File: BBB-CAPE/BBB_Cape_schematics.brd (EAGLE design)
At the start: 160 x 100 mm, 81 parts, among them IC1 EEPROM-I2CSMD, SW2 219-02

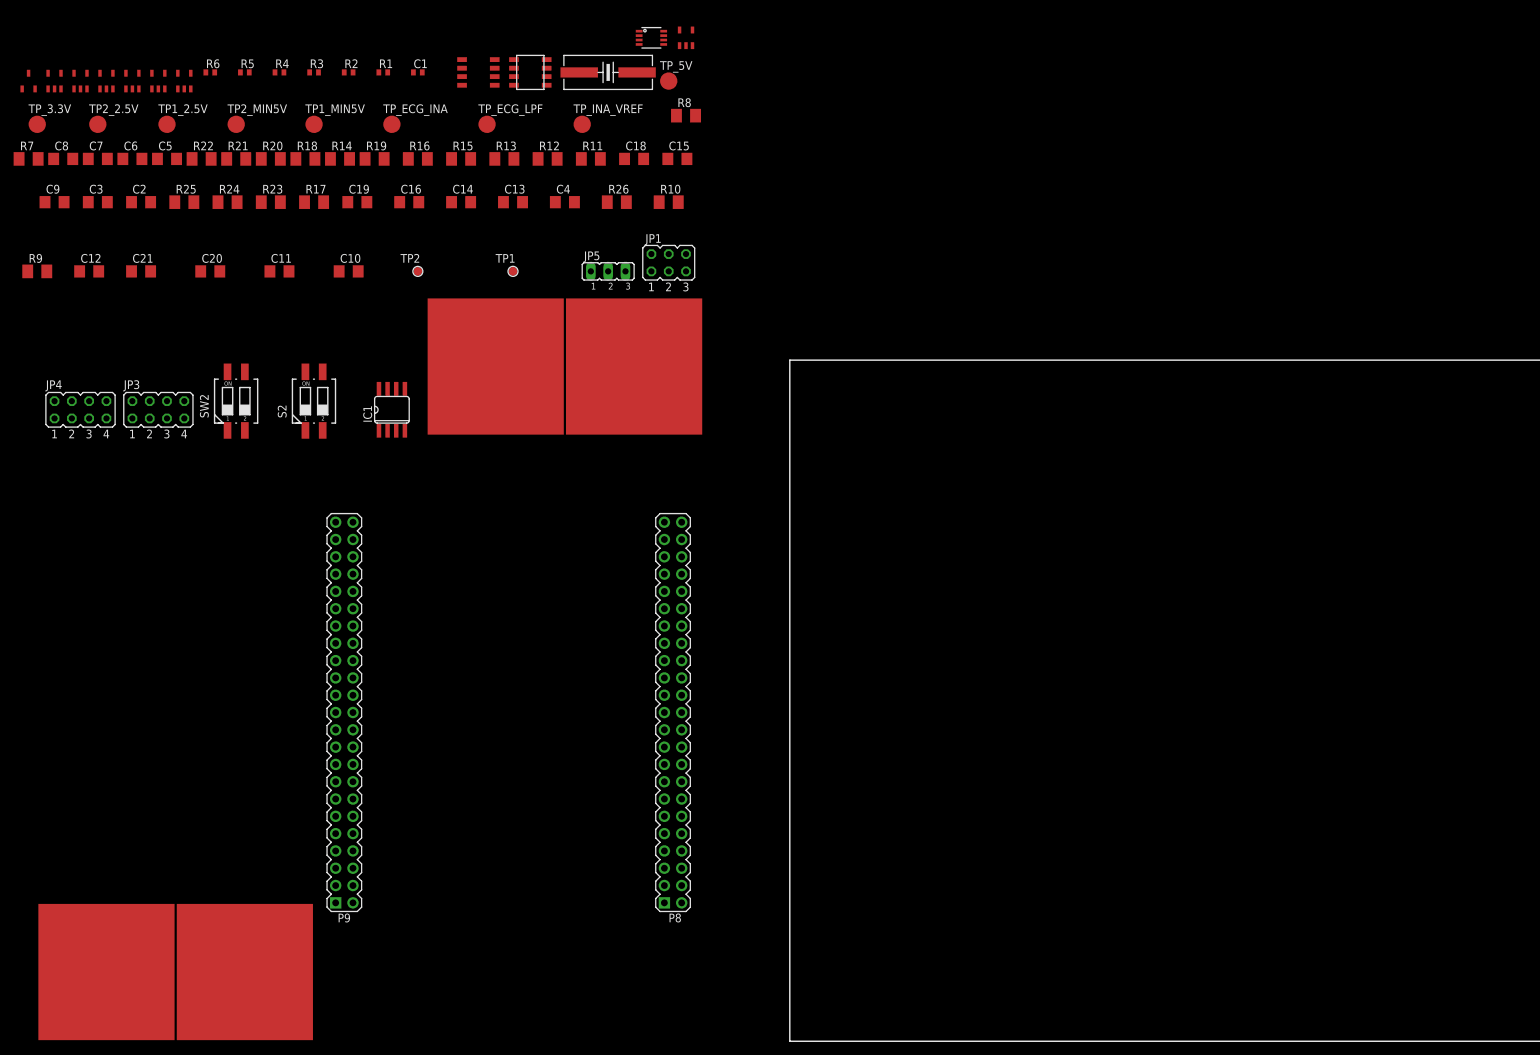
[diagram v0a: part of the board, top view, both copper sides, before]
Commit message: Placement of components in BBB_Cape_schematics.brd, removed ERC erros in BBB_Cape_schematics.sch and Add sign in INA129 to identify pin no 1 in Components.lbr
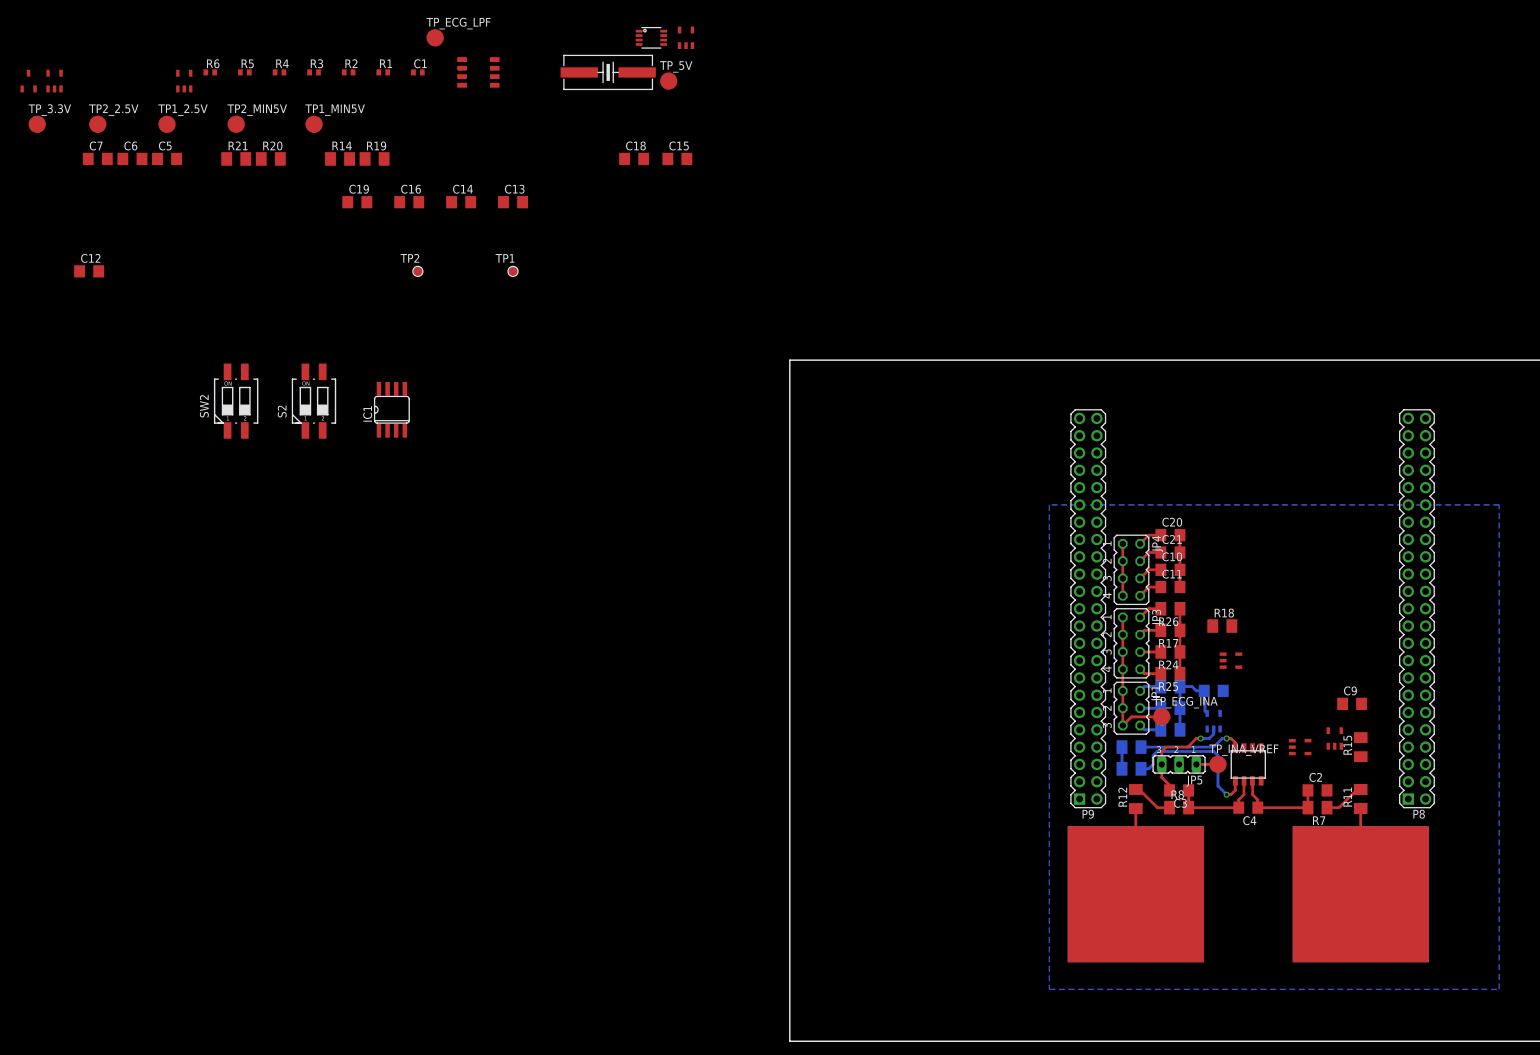
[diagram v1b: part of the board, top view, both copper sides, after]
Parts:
- U$4: device Components:INA129 -> Components:INA129@1
- moved R7 211.9 mm to (77.5, 34.3), turned to 180 degrees
- moved U$12 204.5 mm to (80.0, 44.5)
- moved C9 204.2 mm to (82.5, 49.5)
- moved U$11 197.4 mm to (74.9, 43.2), turned to 270 degrees
- moved C2 193.1 mm to (77.5, 36.8)
- moved U$13 189.1 mm to (64.8, 55.9), turned to 270 degrees
- moved C8 186.1 mm to (62.2, 51.4), flipped to the bottom
- moved U$17 184.5 mm to (83.8, 21.6)
- moved U$9 181.2 mm to (62.2, 47.0), flipped to the bottom
- moved C3 180.7 mm to (57.1, 36.8), turned to 180 degrees
- moved R9 176.5 mm to (50.2, 40.0), flipped to the bottom, turned to 180 degrees
- moved R16 167.3 mm to (83.8, 35.6), flipped to the bottom, turned to 270 degrees
- moved R22 162.0 mm to (55.9, 52.1), flipped to the bottom, turned to 180 degrees
- moved R25 160.5 mm to (55.9, 54.0), turned to 180 degrees
- moved R15 157.8 mm to (83.8, 43.2), turned to 90 degrees
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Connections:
- net N$23: now also U$17.P$1; no longer U$16.P$1
- net N$24: now also U$16.P$1; no longer U$17.P$1
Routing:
- net N$3: track 0.00 -> 22.6 mm, vias 0 -> 1
- net N$11: track 0.00 -> 22.1 mm
- net N$18: track 0.00 -> 17.1 mm
- net GND: track 0.00 -> 15.6 mm, vias 0 -> 1
- net N$4: track 0.00 -> 15.4 mm, vias 0 -> 1
- net N$2: track 0.00 -> 14.2 mm
- net N$1: track 0.00 -> 14.2 mm
- net N$12: track 0.00 -> 13.6 mm
- net N$24: track 0.00 -> 12.6 mm
- net N$23: track 0.00 -> 12.6 mm
- net ECG_LPF: track 0.00 -> 7.62 mm
- net N$8: track 0.00 -> 6.06 mm
- net N$7: track 0.00 -> 5.37 mm
- net N$42: track 0.00 -> 3.57 mm
- net N$40: track 0.00 -> 3.57 mm
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- added copper zone on layer 16, net GND
